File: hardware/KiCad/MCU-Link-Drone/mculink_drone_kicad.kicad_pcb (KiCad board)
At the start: 2 copper layers, 57.9 x 39.9 mm, 108 parts, among them J1 Pixhawk Debug Full, J2 Pixhawk_Debug_Mini, J3 Jumper_2_Open, J4 Jumper_2_Open, J5 Jumper_2_Open, J6 Conn_02x05_Odd_Even, J7 1x3pos, 100mil pitch, J8 DCD-LZ_Debug, J9 USB4110-GF-A_REVB, SW1 KMR221GLFS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

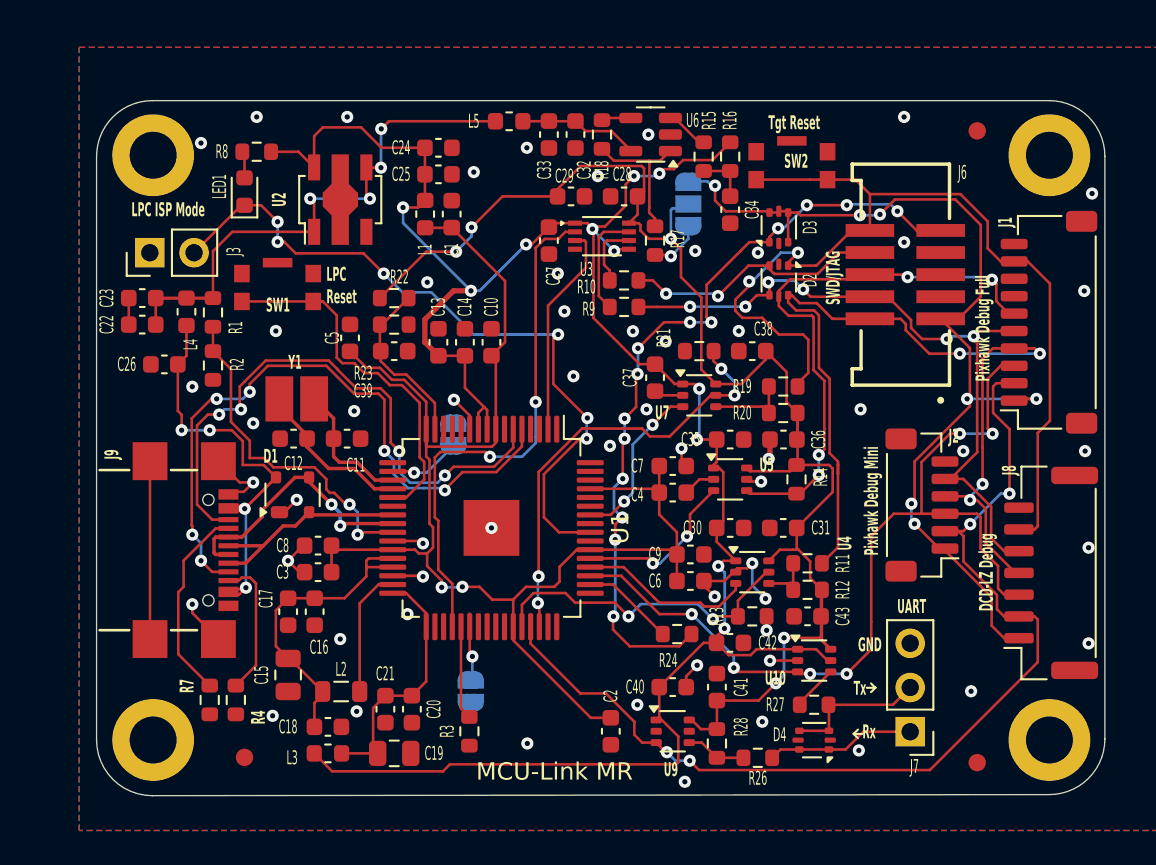
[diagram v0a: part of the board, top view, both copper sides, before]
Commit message: added JST-GH for UART
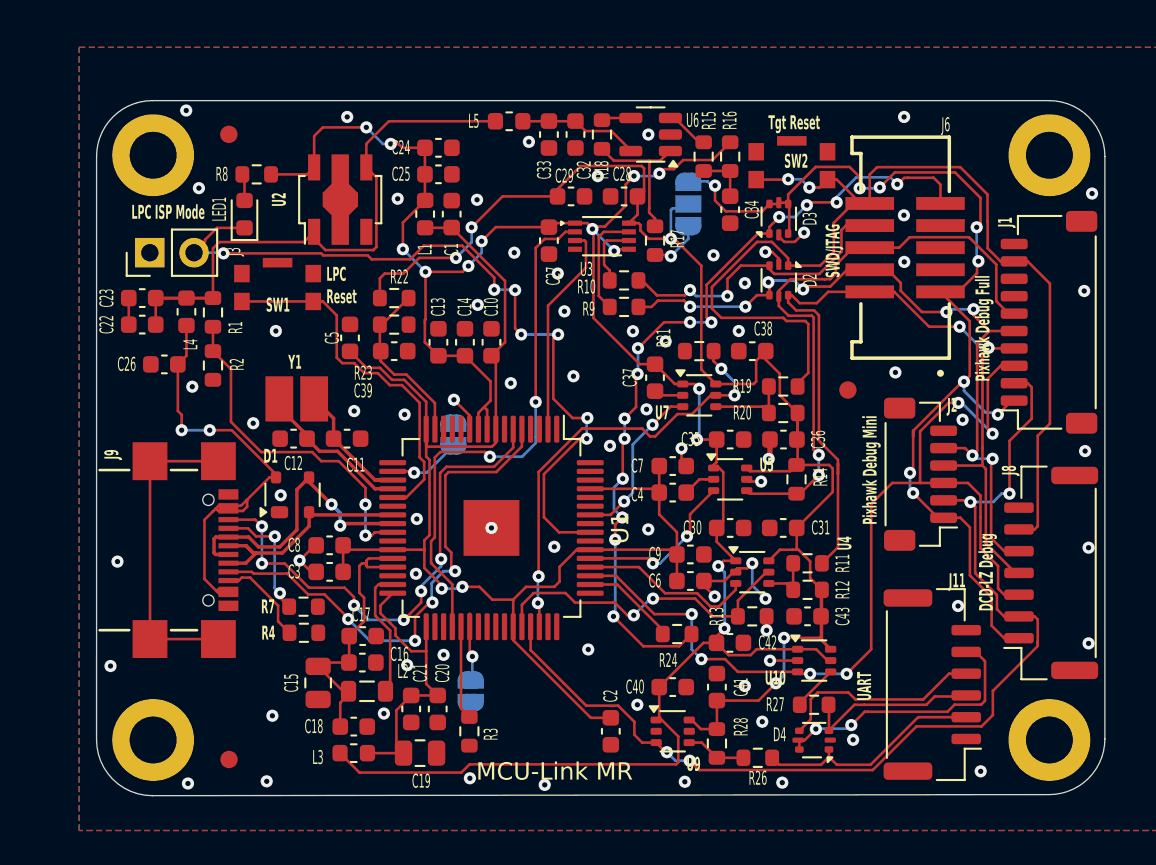
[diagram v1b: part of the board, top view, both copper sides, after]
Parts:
- removed J7: 1x3pos, 100mil pitch, Connector_PinHeader_2.54mm:PinHeader_1x03_P2.54mm_Vertical
- added J11: Conn_01x06_MountingPin, Connector_JST:JST_GH_BM06B-GHS-TBT_1x06-1MP_P1.25mm_Vertical, F.Cu at (212.0, 111.6)
- moved FID3 43.0 mm to (171.6, 80.0)
- moved FID2 22.7 mm to (207.2, 94.7)
- moved R7 7.60 mm to (175.9, 107.1), turned to 180 degrees
- moved R4 5.49 mm to (175.9, 108.6), turned to 180 degrees
- moved C16 5.17 mm to (179.3, 110.3), turned to 0 degrees
- moved C17 3.10 mm to (179.3, 108.8), turned to 0 degrees
- moved C15 1.78 mm to (176.7, 111.5)
- moved J2 1.77 mm to (211.3, 99.5)
- moved J6 1.55 mm to (210.5, 86.5)
- moved C18 1.48 mm to (178.8, 114.0)
- moved C19 1.48 mm to (182.6, 115.6)
- moved C20 1.48 mm to (183.6, 113.0)
- moved C21 1.48 mm to (182.1, 113.0)
- moved L2 1.48 mm to (179.5, 112.0)
- moved L3 1.48 mm to (178.8, 115.6)
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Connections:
- D4 pad 4: Net-(D4B-K2) -> Net-(D4C-K3)
- D4 pad 5: unconnected-(D4D-K4-Pad5) -> Net-(D4D-K4)
- D4 pad 6: Net-(D4A-K1) -> Net-(D4D-K4)
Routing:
- net Net-(D4D-K4): track 0.00 -> 15.8 mm, vias 0 -> 2
- net Net-(D4C-K3): track 0.00 -> 12.0 mm
- net LPC_SWDIO: track 38.0 -> 29.7 mm, vias 6 -> 4
- net /Debug interface/IF_RST: track 57.9 -> 64.0 mm
- net LPC_SWDCLK: track 34.3 -> 29.2 mm, vias 4 -> 6
- net FCO_TARGET_TXD: track 51.5 -> 56.4 mm
- net Net-(D4A-K1): track 8.55 -> 13.2 mm
- net /Debug interface/IF_SWDIO: track 53.9 -> 49.3 mm, vias 4 -> 2
- net Net-(J9-CC1): track 11.4 -> 7.25 mm, vias 0 -> 2
- net /Debug interface/VTARGET: track 56.9 -> 60.7 mm, vias 7 -> 9
- net PIO0_5-ISP_EN-LED1_CTRL: track 42.4 -> 45.9 mm, vias 6 -> 7
- net /Debug interface/IF_SWO: track 32.7 -> 35.1 mm, vias 4 -> 2
- net /Debug interface/IF_TDI: track 15.2 -> 17.4 mm
- net GND: track 45.3 -> 43.2 mm, vias 58 -> 73
- net Net-(J9-CC2): track 7.55 -> 5.42 mm
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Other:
- board text removed: "GND"
- board text removed: "Rx"
- board text removed: "Tx"

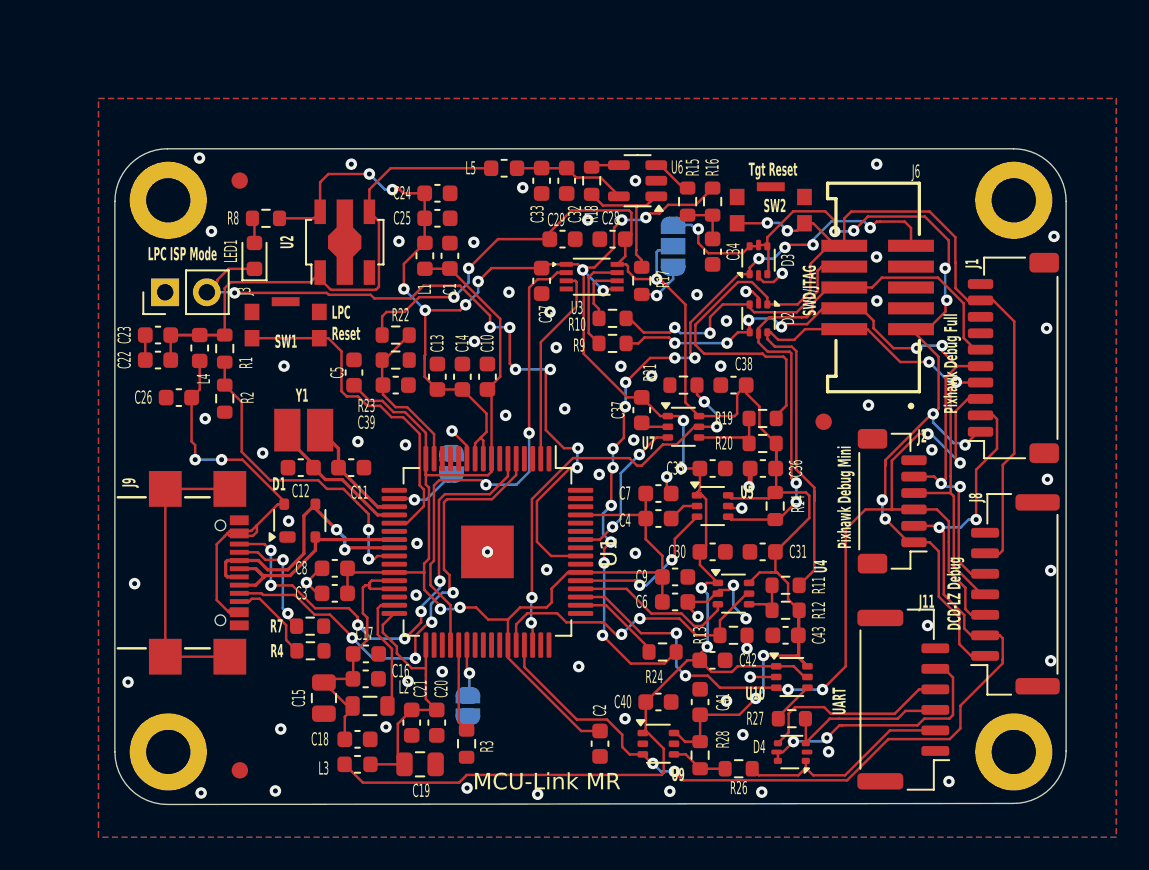
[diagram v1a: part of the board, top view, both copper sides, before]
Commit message: production files for V0.1
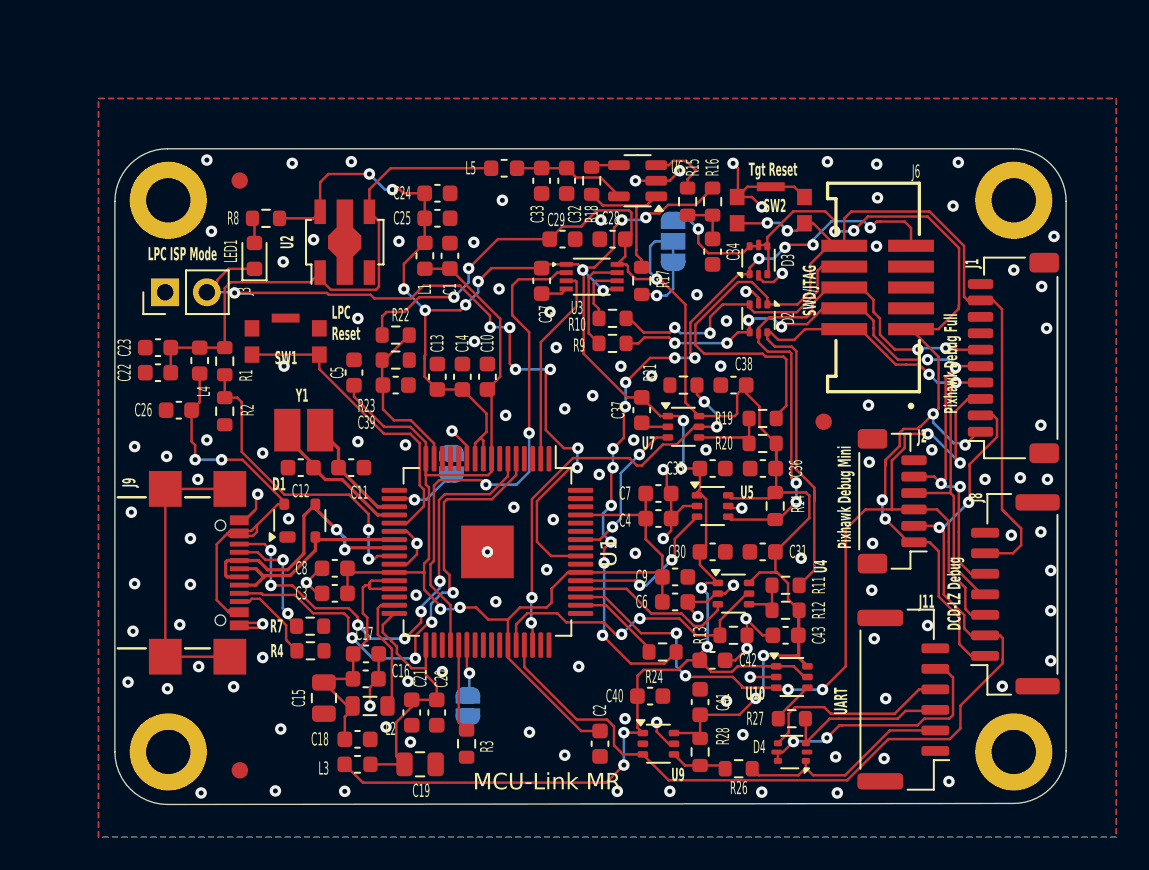
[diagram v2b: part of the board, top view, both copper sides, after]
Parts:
- moved SW1 1.00 mm to (174.4, 89.8)
- moved L4 0.77 mm to (169.2, 91.0)
- moved C22 0.77 mm to (166.6, 91.7)
- moved C23 0.77 mm to (166.6, 90.2)
- moved C26 0.77 mm to (167.9, 94.0)
- moved R1 0.77 mm to (170.7, 91.0)
- moved R2 0.77 mm to (170.7, 94.0)
- moved C40 0.62 mm to (196.6, 111.4)
- moved C20 0.62 mm to (183.6, 112.4)
- moved C21 0.62 mm to (182.1, 112.4)
- moved JP1 0.30 mm to (198.0, 83.7)
- moved R28 0.20 mm to (199.6, 114.8)
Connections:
- JP1 pad 1: Net-(JP1-A) -> IF_VREF
- R17 pad 1: Net-(JP1-A) -> IF_VREF
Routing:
- net GND: track 43.2 -> 75.2 mm, vias 73 -> 124
- net IF_VREF: track 87.9 -> 93.3 mm, vias 5 -> 6
- net Net-(JP1-A): track 3.05 -> 0.00 mm, vias 1 -> 0
- net +5V: track 35.6 -> 33.1 mm
- net LPC_RST: track 20.8 -> 19.1 mm
- net Net-(U6-+): track 2.49 -> 4.05 mm
- net DBGIF_TCK_SWCLK: track 30.5 -> 32.1 mm
- net /Debug interface/VTARGET: track 60.7 -> 62.2 mm, vias 9 -> 7
- net /Debug interface/IF_RST: track 64.0 -> 65.2 mm
- net /McuLink Power and USB/USB_VBUS: track 26.3 -> 25.5 mm
- net +3V3: track 125.7 -> 125.0 mm, vias 14 -> 16
- net FC0_TARGET_RXD: track 60.3 -> 59.7 mm, vias 4 -> 2
- net /Debug interface/IF_SWO: track 35.1 -> 34.5 mm, vias 2 -> 4
- net LPC_SWDIO: track 29.7 -> 30.2 mm
- net FCO_TARGET_TXD: track 56.4 -> 56.9 mm
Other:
- board text added: "V0.1 26-March-2024 Erich Styger"

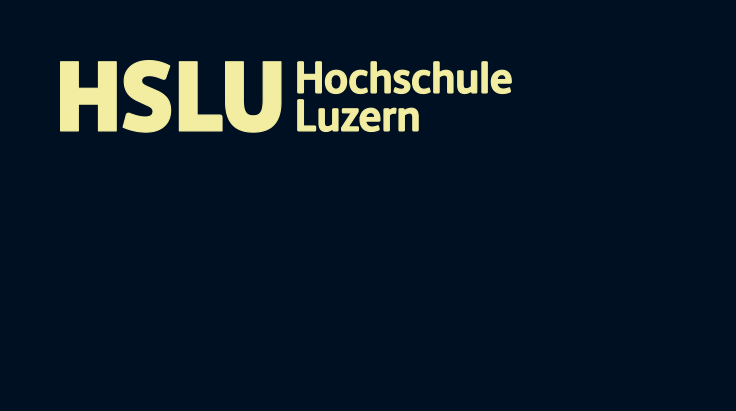
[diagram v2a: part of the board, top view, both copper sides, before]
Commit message: fixed silkscreen
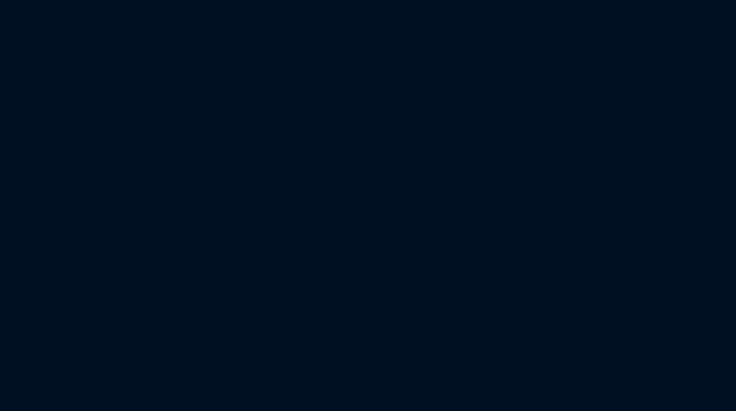
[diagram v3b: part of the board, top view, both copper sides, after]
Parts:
- L6: moved to B.Cu
- moved L6 210.2 mm to (194.3, 89.9), turned to 180 degrees

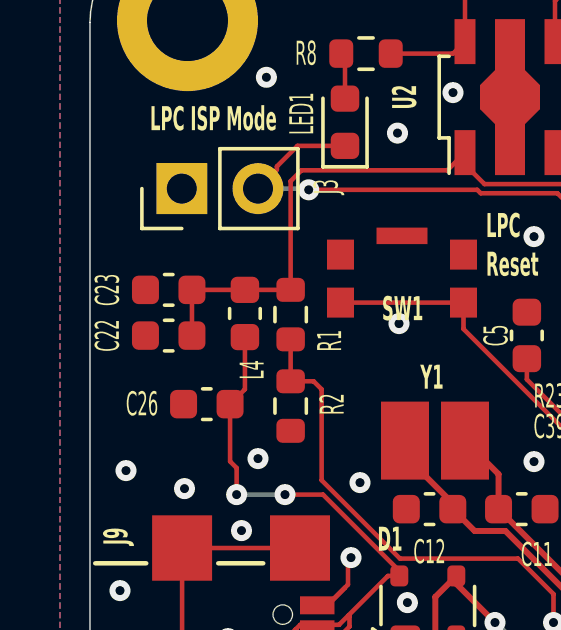
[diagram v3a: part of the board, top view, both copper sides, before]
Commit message: updated schematics
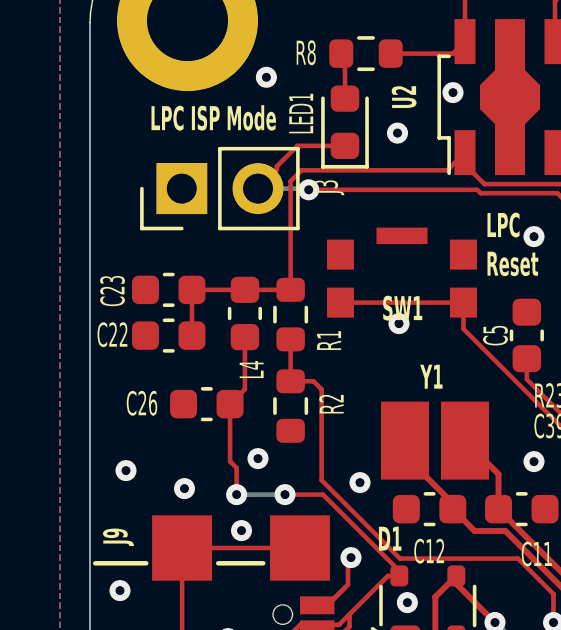
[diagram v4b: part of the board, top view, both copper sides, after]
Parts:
- C1: value 4U7 -> 4.7uF
- C18: value UL-22U -> 22u
- J11: value Conn_01x06_MountingPin -> JST-GH_BM06B
- L2: value 4U7 -> 4u7
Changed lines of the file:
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@@
 			)
 		)
-		(property "Value" "4U7"
+		(property "Value" "4.7uF"
 			(at 0 1.43 90)
 			(layer "F.Fab")
@@
 		(tags "capacitor")
 		(property "Reference" "C22"
-			(at 2.032 0 90)
+			(at 1.864 0 180)
 			(layer "F.SilkS")
 			(effects
@@
 		(tags "capacitor")
 		(property "Reference" "C23"
-			(at 2.032 0 90)
+			(at 1.844 -0.035 -90)
 			(layer "F.SilkS")
 			(effects
@@
 			)
 		)
-		(property "Value" "4U7"
+		(property "Value" "4u7"
 			(at 0 1.55 0)
 			(layer "F.Fab")
@@
 			)
 		)
-		(property "Value" "UL-22U"
+		(property "Value" "22u"
 			(at 0 1.43 0)
 			(layer "F.Fab")
@@
 			)
 		)
-		(property "Value" "Conn_01x06_MountingPin"
+		(property "Value" "JST-GH_BM06B"
 			(at 0 4 -90)
 			(layer "F.Fab")
